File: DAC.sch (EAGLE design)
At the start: 101 parts, among them IC1 LM2662, IC2 PCM1793, IC3 OPA2134PA, IC4 LMH6643, J1 USBSMD, J2 RCJ-21XXMILL, U1 LDO-TPS78233, U2 PCM2707, Y1 12MHz/20pF

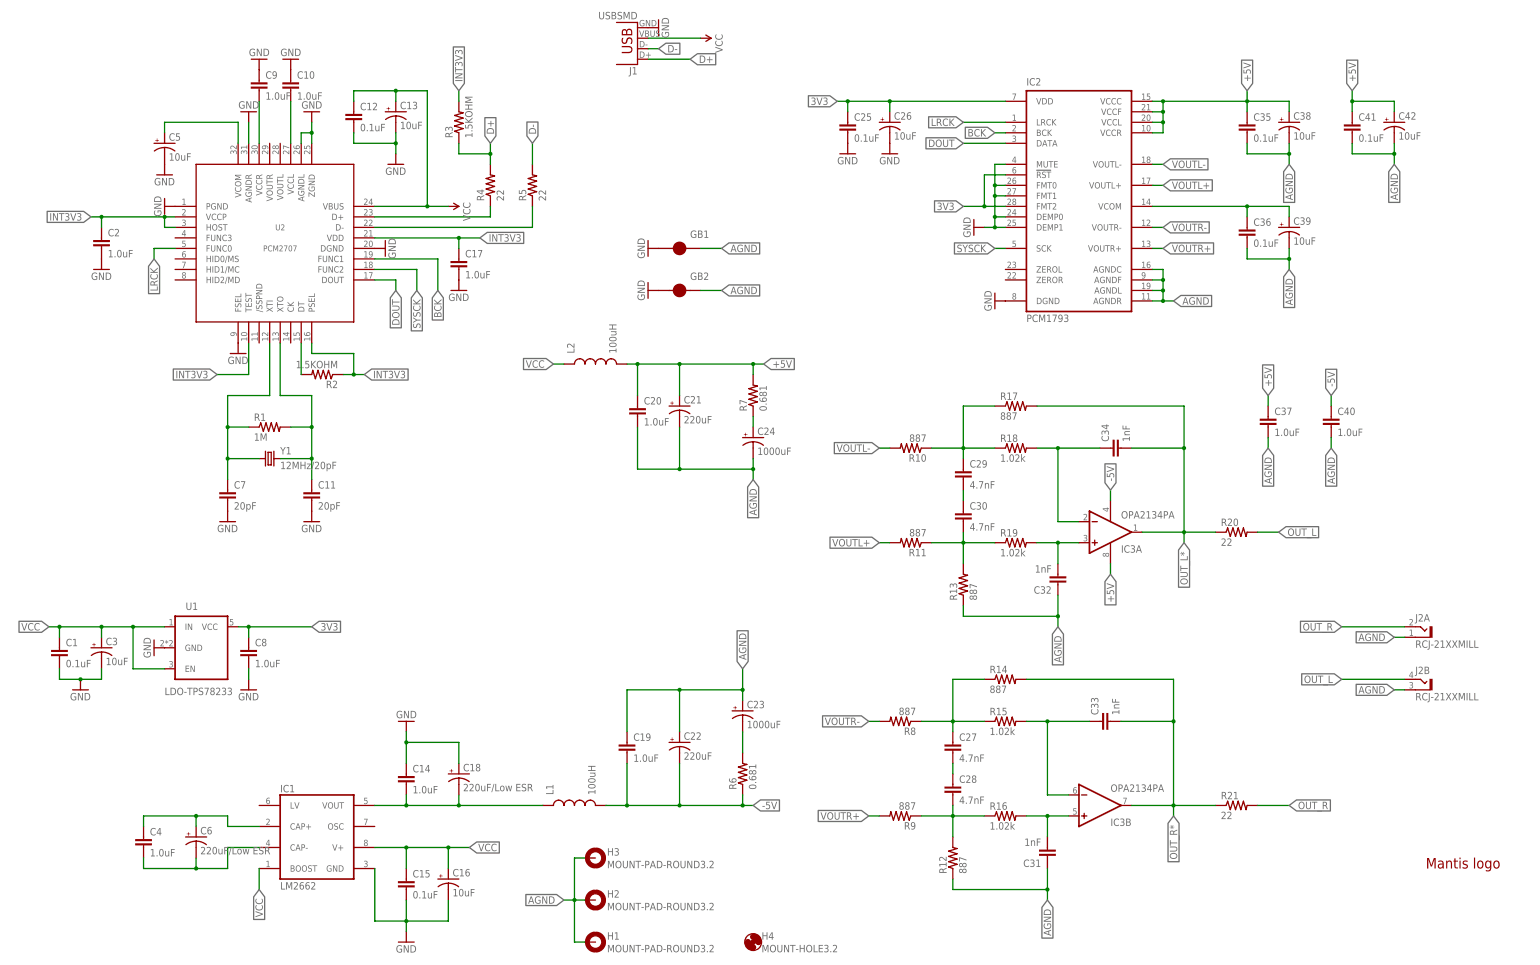
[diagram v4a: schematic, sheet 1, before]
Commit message: PCB layout closer to guidelines
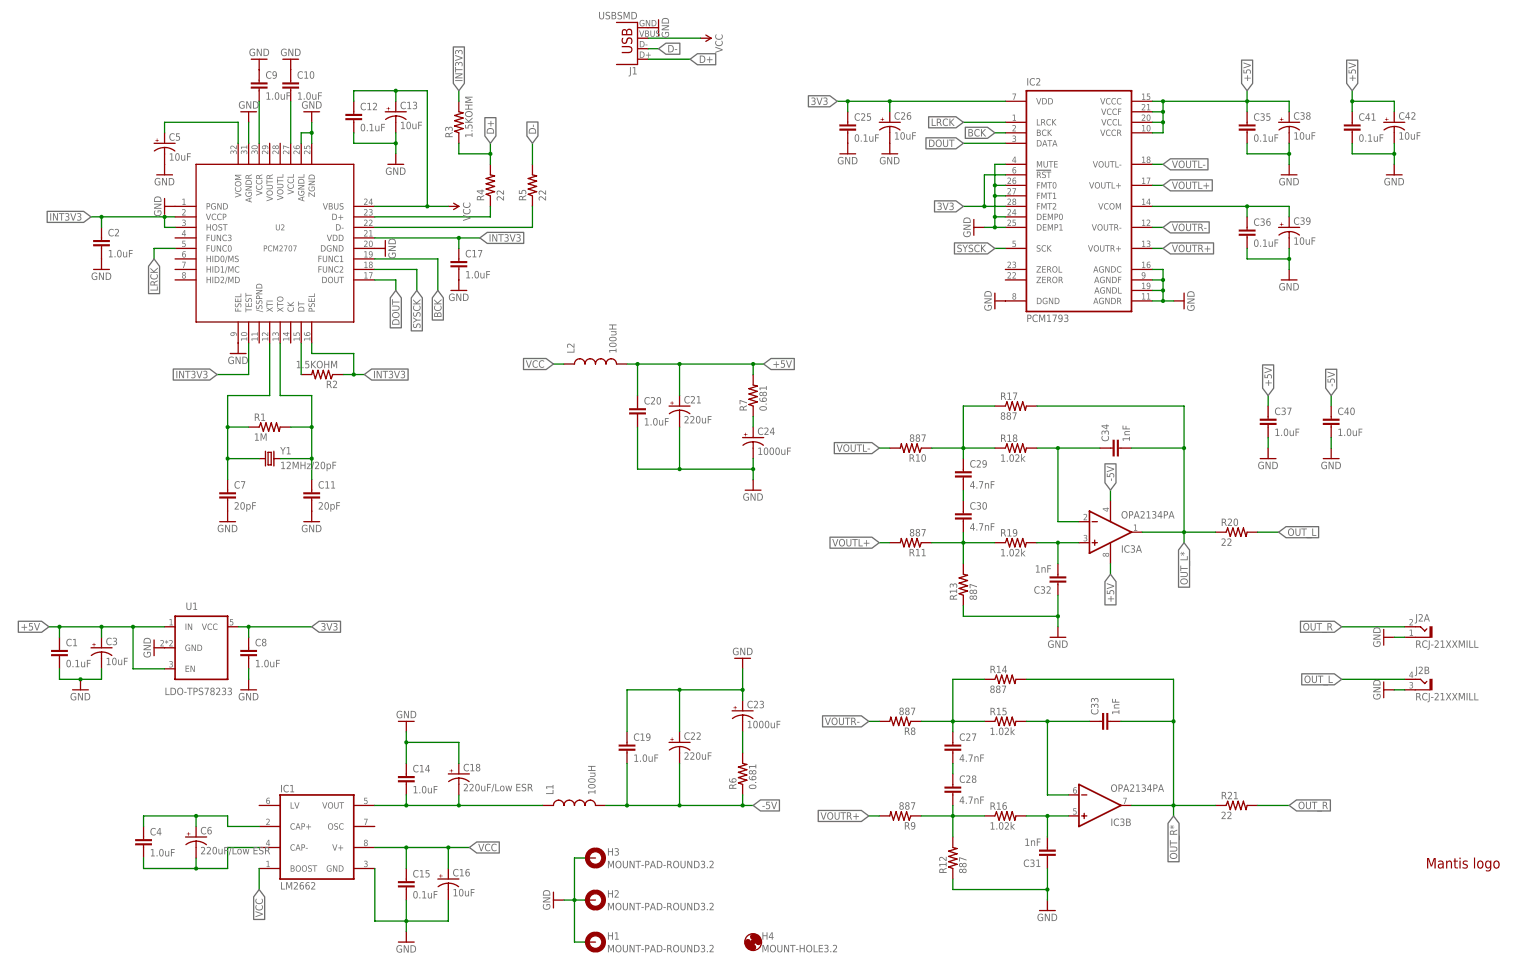
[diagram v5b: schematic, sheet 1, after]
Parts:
- removed GB1, GB2: COPPER-BRIDGE, my:COPPER-BRIDGE
- R23, R25, R26, R28: value 100k -> 47k
- R24, R27: value 56k -> 24k
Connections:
- removed net AGND: C19.1, C20.2, C21.-, C22.+, C23.+, C24.-, C31.1, C32.1, C35.2, C36.2, C37.2, C38.-, C39.-, C40.2, C41.2, C42.-, C44.1, C47.+, C48.2, C49.-, C50.2, C52.1, GB1.2, GB2.2, H1.MOUNT, H2.MOUNT, H3.MOUNT, IC2.AGNDC, IC2.AGNDF, IC2.AGNDL, IC2.AGNDR, J2A.S, J2B.S, J3.SLEEVE, R12.1, R13.1, R22A.A, R22B.A, R23.1, R26.1
- net +5V: now also C1.1, C3.+, U1.EN, U1.IN
- net GND: now also C19.1, C20.2, C21.-, C22.+, C23.+, C24.-, C31.1, C32.1, C35.2, C36.2, C37.2, C38.-, C39.-, C40.2, C41.2, C42.-, C44.1, C47.+, C48.2, C49.-, C50.2, C52.1, H1.MOUNT, H2.MOUNT, H3.MOUNT, IC2.AGNDC, IC2.AGNDF, IC2.AGNDL, IC2.AGNDR, J2A.S, J2B.S, J3.SLEEVE, R12.1, R13.1, R22A.A, R22B.A, R23.1, R26.1; no longer GB1.1, GB2.1
- net VCC: no longer C1.1, C3.+, U1.EN, U1.IN
